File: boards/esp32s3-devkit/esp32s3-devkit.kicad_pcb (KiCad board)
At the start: 4 copper layers, 59.3 x 38 mm, 37 parts, among them J1 Conn_01x17_Pin, J2 Conn_01x17_Pin, J3 USB_C_Receptacle_USB2.0_16P, Q1 AO3401A, SW1 MK-12C03-G015, SW2 RESET, SW3 BOOT, U1 TPS63070RNMR, U2 ESP32-S3-WROOM-1-N16, U3 USBLC6-2SC6

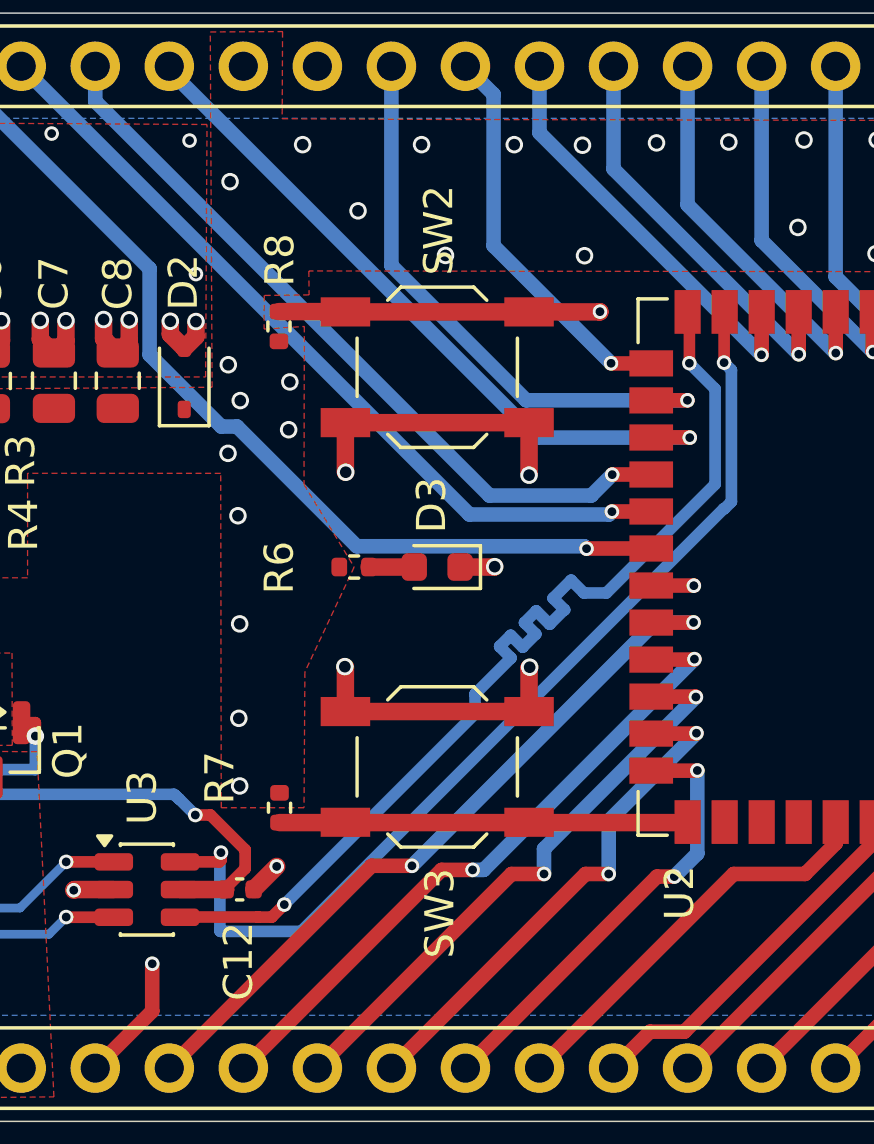
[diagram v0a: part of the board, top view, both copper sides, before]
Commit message: fix(esp32s3-devkit): retarget SW2/SW3 to TS-1187A footprint for JLC assembly (#115)
The RESET/BOOT buttons used Button_Switch_SMD:SW_SPST_TL3342, which does
not correspond to a JLCPCB-stocked tactile switch — JLC auto-matched it to
TS-1187A (C318884, their Basic go-to) but flagged it because the TL3342
footprint (pads at +/-3.15mm X, +/-1.90mm Y) does not fit the 5.1mm part,
so the buttons could not be placed.

Swap both to Button_Switch_SMD:SW_Push_1P1T_XKB_TS-1187A, the footprint
made for that exact part. Pad centers move <=0.15mm (+/-3.00mm / +/-1.88mm)
and pad numbering/nets are preserved, so routing is unchanged; ERC, DRC,
schematic parity, fab-DRC, and validate all pass. JLC now matches C318884
cleanly and assembles the buttons.

Co-authored-by: Claude Fable 5 <noreply@anthropic.com>
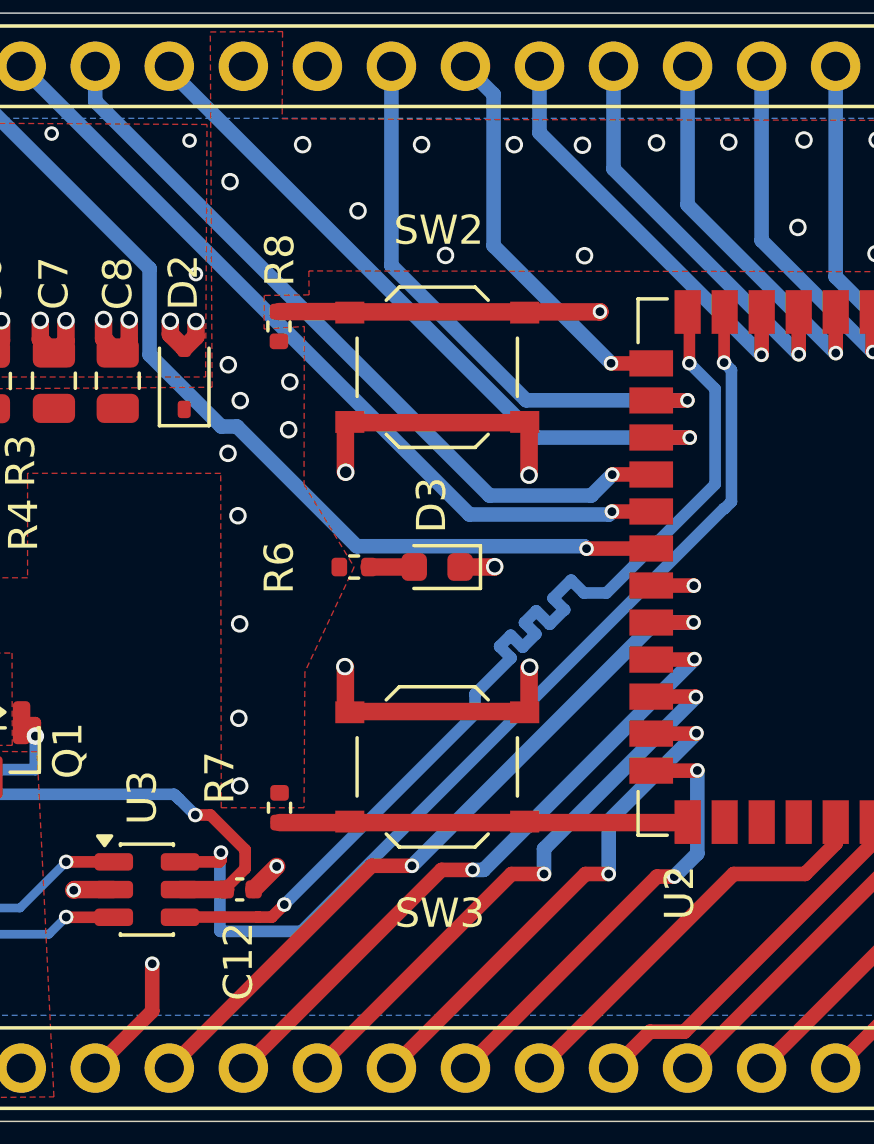
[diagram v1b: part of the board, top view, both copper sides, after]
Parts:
- SW2, SW3: footprint Button_Switch_SMD:SW_SPST_TL3342 -> Button_Switch_SMD:SW_Push_1P1T_XKB_TS-1187A

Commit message: fix(esp32s3-devkit): connect VBAT to Q1 drain — board shipped with a dead battery input
The assembled boards do not power on. Root cause: Q1's drain pad (/VBAT, the
battery input) has no copper on it, so the battery never reaches the reverse-
protection FET. Confirmed on hardware — injecting battery+ at the /PFET net
downstream of Q1 boots the board normally.

How it happened:
- The entire battery path (/VBAT, /PFET, /VBAT_SW) was routed with copper pours
  and ZERO tracks.
- The /VBAT pour is pinched to 0.17 mm against the neighbouring /PFET pour right
  where Q1's drain sits, so the fill never reached the pad.
- KiCad DRC reported "0 unconnected items" on every run: the ratsnest treats a
  pad as zone-connected when the zone OUTLINE overlaps it, even though the
  FILLED copper does not.

Fix: route /VBAT explicitly, J1.2 -> Q1.3, 0.8 mm on F.Cu, inside the existing
VBAT corridor. /PFET and /VBAT_SW are left as-is: both verified to have their
pads inside filled copper, and proven conducting on the hardware.

Guard so this cannot ship again: scripts/ci/check_copper_connectivity.py asserts
the real invariant geometrically — every pad on a multi-pad net must be inside
same-net filled copper or touched by a same-net track/via. Pads sharing a number
in one footprint (module thermal pads with heatsink vias, switch double pins)
count as one node. Wired into `make check` and the CI drc job.

Verified: the guard FAILS on the pre-fix board naming exactly Q1.3, and PASSES
on the fixed board and on tps63070-breakout. ERC, DRC, parity, fab-DRC all pass.

Co-Authored-By: Claude Fable 5 <noreply@anthropic.com>
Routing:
- net /VBAT: track 0.00 -> 10.0 mm
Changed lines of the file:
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@@
+	)
+	(segment
+		(start 128.515 119.09)
+		(end 127.5775 109.115)
+		(width 0.8)
+		(layer "F.Cu")
+		(net "/VBAT")
 	)
 	(segment
